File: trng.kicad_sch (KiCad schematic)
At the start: 22 parts, among them J1 USB_A, U1 FT240XQ, U2 MC74VHC1G66DFT1G, U3 MC74VHC1G66DFT1G, U4 TSV912IQ2T, U5 TS3022IYST

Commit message: Update schematic pdf, add BOM
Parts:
- J1: value USB_A -> 0480372200
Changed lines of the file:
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@@
     (in_bom yes) (on_board yes) (fields_autoplaced)
     (property "Reference" "J1" (id 0) (at 33.02 46.99 0))
-    (property "Value" "USB_A" (id 1) (at 33.02 49.53 0))
+    (property "Value" "0480372200" (id 1) (at 33.02 49.53 0))
     (property "Footprint" "trng-parts:USB-A-PLUG" (id 2) (at 36.83 60.96 0)
       (effects (font (size 1.27 1.27)) hide)
@@
     )
     (path "/9d4b38cb-2303-4d75-bfcc-57af2fbae303"
-      (reference "J1") (unit 1) (value "USB_A") (footprint "trng-parts:USB-A-PLUG")
+      (reference "J1") (unit 1) (value "0480372200") (footprint "trng-parts:USB-A-PLUG")
     )
     (path "/50604856-de26-4b87-8069-342618e39e5f"

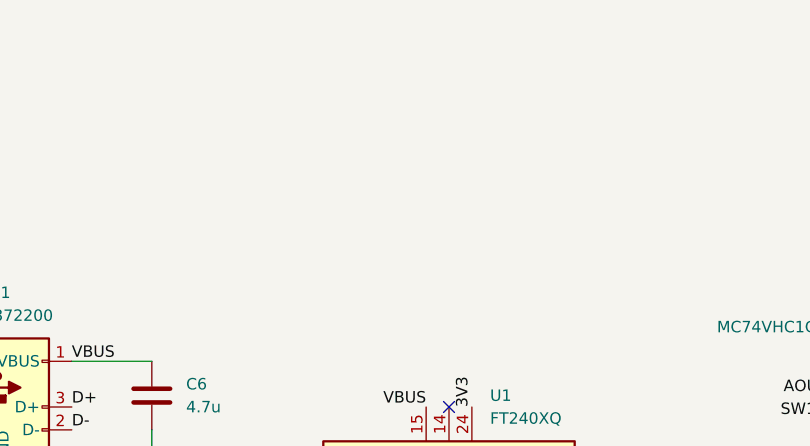
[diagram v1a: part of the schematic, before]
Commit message: Add test header and recreate production data
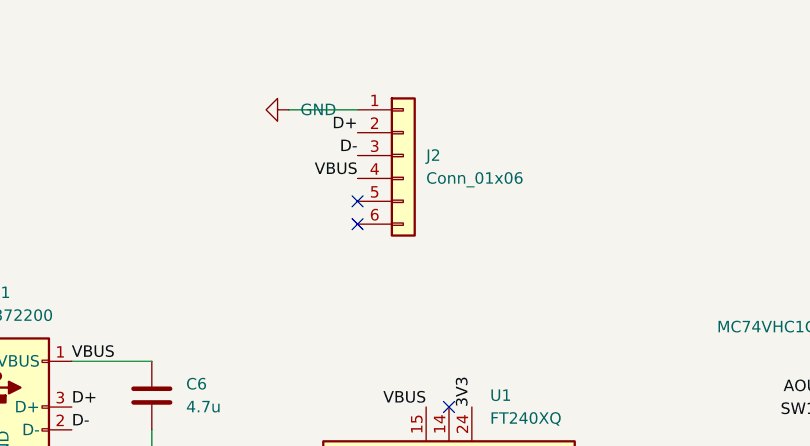
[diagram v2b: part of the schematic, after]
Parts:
- added J2: Conn_01x06, cl6:nitro_programming_header, symbol Connector_Generic:Conn_01x06
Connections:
- net D+: now also J2.2 (Pin_2)
- net D-: now also J2.3 (Pin_3)
- net GND: now also J2.1 (Pin_1)
- net VBUS: now also J2.4 (Pin_4)
- no-connect marks 9 -> 11
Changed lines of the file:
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@@
   )
   (no_connect (at 100.33 105.41))
+  (no_connect (at 72.39 39.37))
   (no_connect (at 82.55 59.69))
   (no_connect (at 100.33 74.93))
@@
   (no_connect (at 100.33 107.95))
   (no_connect (at 100.33 92.71))
+  (no_connect (at 72.39 36.83))
   (no_connect (at 100.33 85.09))
   (no_connect (at 100.33 82.55))
@@
     (stroke (width 0) (type default) (color 0 0 0 0))
   )
+  (wire (pts (xy 64.77 26.67) (xy 72.39 26.67))
+    (stroke (width 0) (type default) (color 0 0 0 0))
+  )
   (wire (pts (xy 172.72 74.93) (xy 172.72 71.12))
     (stroke (width 0) (type default) (color 0 0 0 0))
@@
     (effects (font (size 1.27 1.27)) (justify left bottom))
   )
+  (label "D-" (at 72.39 31.75 180)
+    (effects (font (size 1.27 1.27)) (justify right bottom))
+  )
   (label "SW2EN" (at 100.33 67.31 0)
     (effects (font (size 1.27 1.27)) (justify left bottom))
@@
     (effects (font (size 1.27 1.27)) (justify left bottom))
   )
+  (label "VBUS" (at 72.39 34.29 180)
+    (effects (font (size 1.27 1.27)) (justify right bottom))
+  )
   (label "COMP2" (at 176.53 123.19 0)
     (effects (font (size 1.27 1.27)) (justify left bottom))
@@
   (label "3V3" (at 135.89 50.8 0)
     (effects (font (size 1.27 1.27)) (justify left bottom))
+  )
+  (label "D+" (at 72.39 29.21 180)
+    (effects (font (size 1.27 1.27)) (justify right bottom))
   )
   (label "3V3" (at 172.72 45.72 0)
@@
     (pin "2")
   )
+  (symbol (lib_id "Connector_Generic:Conn_01x06") (at 77.47 31.75 0) (unit 1)
+    (in_bom yes) (on_board yes) (fields_autoplaced)
+    (property "Reference" "J2" (id 0) (at 80.01 31.7499 0)
+      (effects (font (size 1.27 1.27)) (justify left))
+    )
+    (property "Value" "Conn_01x06" (id 1) (at 80.01 34.2899 0)
+      (effects (font (size 1.27 1.27)) (justify left))
+    )
+    (property "Footprint" "cl6:nitro_programming_header" (id 2) (at 77.47 31.75 0)
+      (effects (font (size 1.27 1.27)) hide)
+    )
+    (property "Datasheet" "~" (id 3) (at 77.47 31.75 0)
+      (effects (font (size 1.27 1.27)) hide)
+    )
+    (pin "1")
+    (pin "2")
+    (pin "3")
+    (pin "4")
+    (pin "5")
+    (pin "6")
+  )
   (symbol (lib_id "Amplifier_Operational:TSV912IQ2T") (at 165.1 102.87 0) (unit 2)
     (in_bom yes) (on_board yes) (fields_autoplaced)
@@
     )
     (property "Datasheet" "" (id 3) (at 33.02 69.85 0)
+      (effects (font (size 1.27 1.27)) hide)
+    )
+    (pin "1")
+  )
+  (symbol (lib_id "power:GND") (at 64.77 26.67 270) (unit 1)
+    (in_bom yes) (on_board yes) (fields_autoplaced)
+    (property "Reference" "#PWR0104" (id 0) (at 58.42 26.67 0)
+      (effects (font (size 1.27 1.27)) hide)
+    )
+    (property "Value" "GND" (id 1) (at 66.04 26.6699 90)
+      (effects (font (size 1.27 1.27)) (justify left))
+    )
+    (property "Footprint" "" (id 2) (at 64.77 26.67 0)
+      (effects (font (size 1.27 1.27)) hide)
+    )
+    (property "Datasheet" "" (id 3) (at 64.77 26.67 0)
       (effects (font (size 1.27 1.27)) hide)
     )
@@
       (reference "#PWR0103") (unit 1) (value "GND") (footprint "")
     )
+    (path "/ee823590-ecbd-4107-bb1f-1a309e1b21af"
+      (reference "#PWR0104") (unit 1) (value "GND") (footprint "")
+    )
     (path "/3ea2f31f-4b80-4b73-8f6c-8aaf56f982a3"
       (reference "C1") (unit 1) (value "220p") (footprint "Capacitor_SMD:C_0603_1608Metric")
@@
       (reference "J1") (unit 1) (value "0480372200") (footprint "trng-parts:USB-A-PLUG")
     )
+    (path "/dea30d29-44e9-47fc-bccc-6928d5c29cea"
+      (reference "J2") (unit 1) (value "Conn_01x06") (footprint "cl6:nitro_programming_header")
+    )
     (path "/50604856-de26-4b87-8069-342618e39e5f"
